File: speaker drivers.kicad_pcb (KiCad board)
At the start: 2 copper layers, 75 x 25.2 mm, 23 parts, among them P1 CONN_01X02

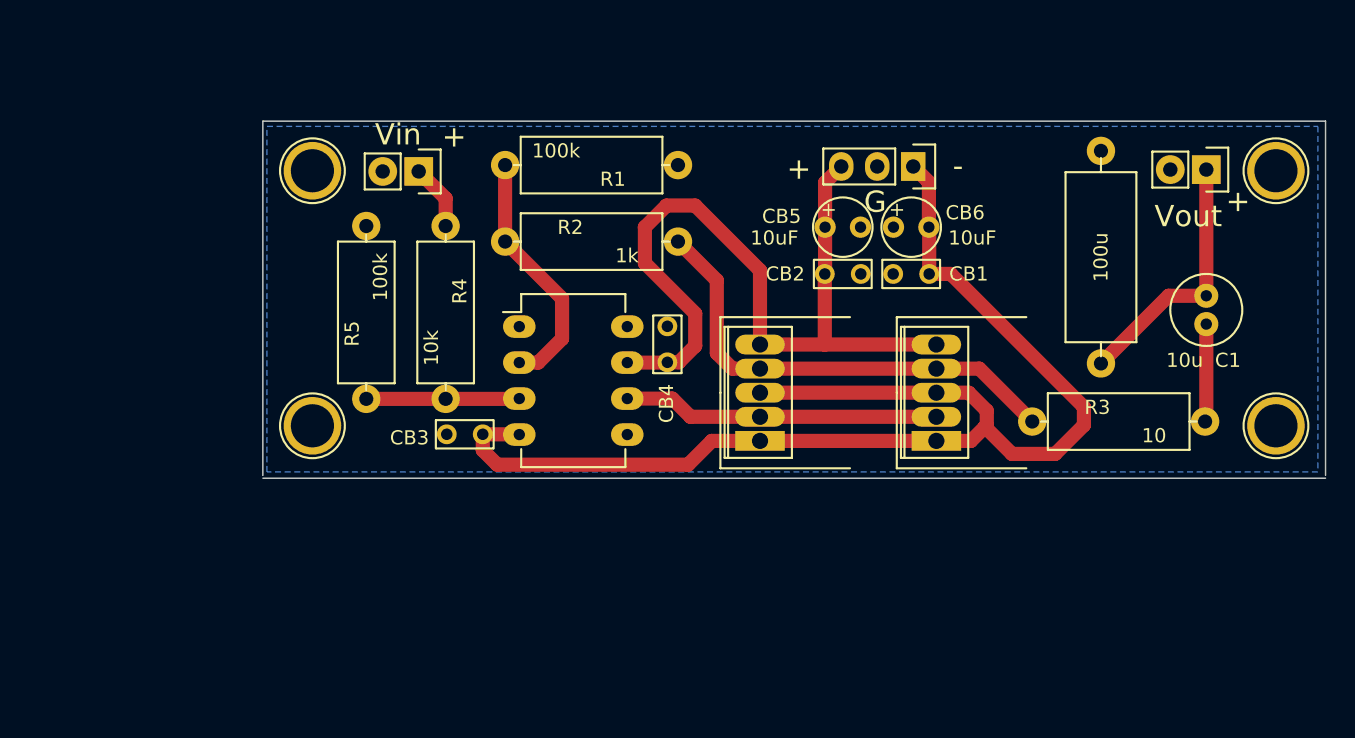
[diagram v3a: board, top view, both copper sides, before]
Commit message: Fixed bug in previous version and updated design
* Inverting and noninverting inputs were swapped in the schematic. Fixed
  this bug.
* Removed the highpass filter that follows the current buffer with a
  highpass filter at the input to the current buffer. Highpass filter
  simply removes DC offset now.
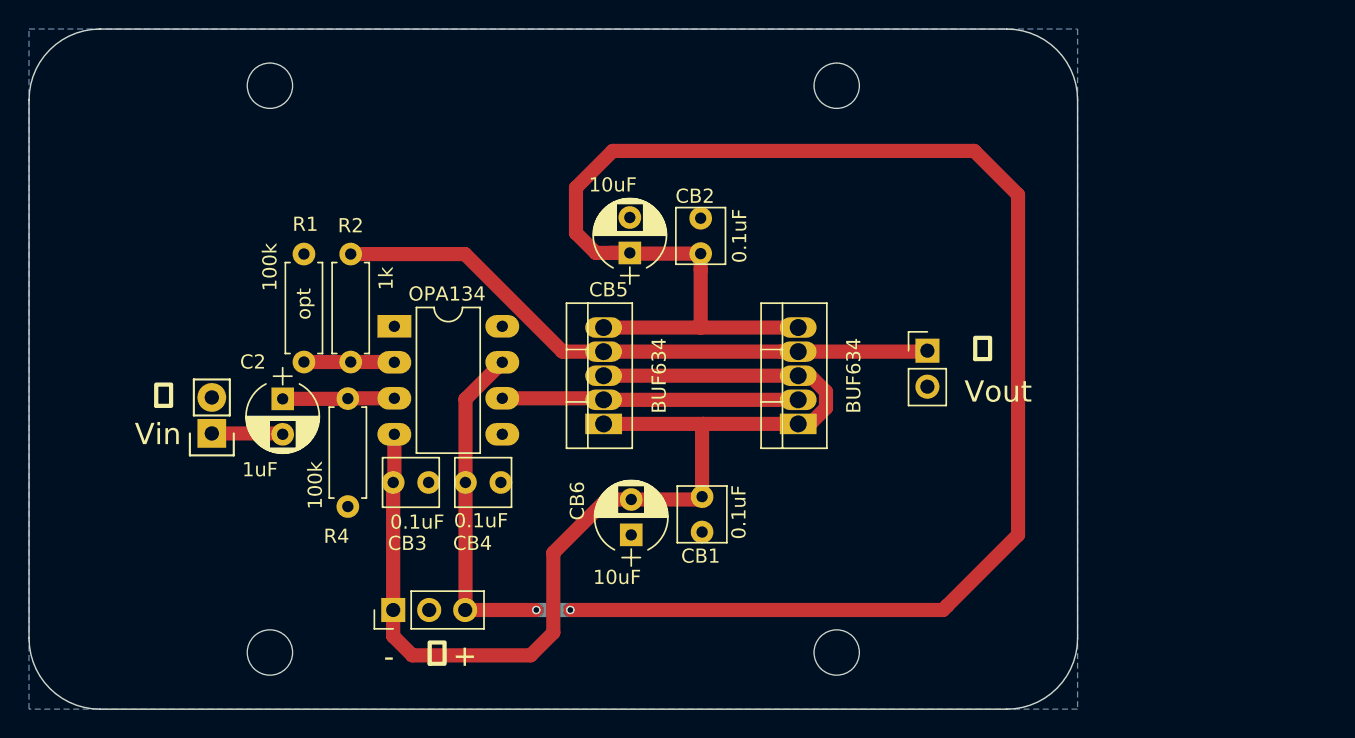
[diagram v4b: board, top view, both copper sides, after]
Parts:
- removed C1: 10u, LBHB:capacitor-D_5mm-L_2mm
- removed L1: 100u, LBHB:inductor-12mm
- removed O1: OPA134, Housings_DIP:DIP-8_W7.62mm_LongPads
- removed R3: 10, LBHB:resistor-13x4mm
- removed R5: 100k, LBHB:resistor-13x4mm
- removed REF** (x4): 1pin, Connect:1pin
- added C2: 1uF, Capacitor_THT:CP_Radial_D5.0mm_P2.50mm, F.Cu at (98.9, 122.1)
- added J1: Conn_01x01, MountingHole:MountingHole_3.2mm_M3, F.Cu at (98.0, 140.0)
- added J2: Conn_01x01, MountingHole:MountingHole_3.2mm_M3, F.Cu at (138.0, 140.0)
- added J3: Conn_01x01, MountingHole:MountingHole_3.2mm_M3, F.Cu at (98.0, 100.0)
- added J4: Conn_01x01, MountingHole:MountingHole_3.2mm_M3, F.Cu at (138.0, 100.0)
- added U1: OPA134, Housings_DIP:DIP-8_W7.62mm_LongPads, F.Cu at (106.8, 117.0)
- B1: footprint LBHB:BUF634_compact_HeatSink -> custom:BUF634T
- B2: footprint LBHB:BUF634_compact_HeatSink -> TO_SOT_Packages_THT:TO-220-5_Vertical
- CB1, CB2, CB3, CB4: footprint LBHB:capacitor-2x4mm-L_2.5mm -> custom:C_Rect_L4.0mm_W3.5mm_P2.50mm
- CB5, CB6: footprint LBHB:capacitor-D_4mm-L_2.4mm -> Capacitor_THT:CP_Radial_D5.0mm_P2.50mm
- P1: footprint Socket_Strips:Socket_Strip_Straight_1x02 -> Conn_PinHeader_2.54mm:PinHeader_1x02_P2.54mm_Vertical
- PWR1: footprint Socket_Strips:Socket_Strip_Straight_1x03 -> Conn_PinHeader_2.54mm:PinHeader_1x03_P2.54mm_Vertical
- R1, R2: footprint LBHB:resistor-13x4mm -> Resistor_THT:R_Axial_DIN0207_L6.3mm_D2.5mm_P7.62mm_Horizontal
- R4: value 10k -> 100k; footprint LBHB:resistor-13x4mm -> Resistor_THT:R_Axial_DIN0207_L6.3mm_D2.5mm_P7.62mm_Horizontal
- moved PWR1 48.2 mm to (106.7, 137.0), turned to 90 degrees
- moved CB6 29.4 mm to (123.5, 131.7), turned to 90 degrees
- moved R1 24.6 mm to (100.4, 119.5), turned to 90 degrees
- moved V1 23.6 mm to (93.9, 124.5), turned to 90 degrees
- moved P1 23.5 mm to (144.4, 118.7), turned to 0 degrees
- moved CB1 22.5 mm to (128.5, 130.2), turned to 270 degrees
- moved R2 17.0 mm to (103.7, 111.9), turned to 270 degrees
- moved CB4 16.2 mm to (113.0, 128.0), turned to 180 degrees
- moved CB5 15.1 mm to (123.4, 111.8), turned to 90 degrees
- moved B2 11.3 mm to (121.5, 123.9)
- moved CB2 10.4 mm to (128.4, 110.6), turned to 90 degrees
- moved B1 10.00 mm to (135.3, 123.9)
- moved R4 9.20 mm to (103.5, 122.1), turned to 270 degrees
- moved CB3 5.10 mm to (108.0, 128.0), turned to 180 degrees
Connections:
- P1 pad 1: Net-(C1-Pad1) -> Net-(B1-Pad4)
- R4 pad 2: Net-(R4-Pad2) -> AGND
- V1 pad 1: Net-(R4-Pad2) -> Net-(C2-Pad2)
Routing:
- net +12V: track 56.5 -> 149.8 mm, vias 0 -> 2
- net Net-(C1-Pad1): track 18.4 -> 0.00 mm
- net Net-(B1-Pad4): track 33.3 -> 44.9 mm
- net Net-(R1-Pad1): track 17.6 -> 6.39 mm
- net -12V: track 91.2 -> 83.8 mm
- net Net-(C1-Pad2): track 6.91 -> 0.00 mm
- net Net-(C2-Pad2): track 0.00 -> 5.11 mm
- net Net-(R4-Pad2): track 4.64 -> 0.00 mm
- net Net-(C2-Pad1): track 10.8 -> 7.90 mm
- net Net-(B1-Pad2): track 22.3 -> 20.9 mm
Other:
- board size 75 x 25.2 mm -> 74 x 48 mm
- net class Default: clearance 0.4 -> 0.16
- rule trace_clearance: 0.4 -> 0.16
- board text added: "Speaker driver Revision 180201 LBHB@OHSU"
- board text added: "opt"
- board text added: "⏚"
- board text removed: "G"
